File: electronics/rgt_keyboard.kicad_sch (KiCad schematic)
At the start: 61 parts, among them J5 Conn_01x05_Female, J6 Conn_01x05_Male, SW30 SW_SPST, SW31 SW_SPST, SW32 SW_SPST, SW33 SW_SPST, SW34 SW_SPST, SW35 SW_SPST, SW36 SW_SPST, SW37 SW_SPST, SW38 SW_SPST, SW39 SW_SPST, SW40 SW_SPST, SW41 SW_SPST, SW42 SW_SPST, SW43 SW_SPST, SW44 SW_SPST, SW45 SW_SPST, SW46 SW_SPST, SW47 SW_SPST, SW48 SW_SPST, SW49 SW_SPST, SW50 SW_SPST, SW51 SW_SPST, SW52 SW_SPST, SW53 SW_SPST, SW54 SW_SPST, SW55 SW_SPST, SW56 SW_SPST, SW57 SW_SPST, SW58 SW_SPST, U3 PCA9675PW

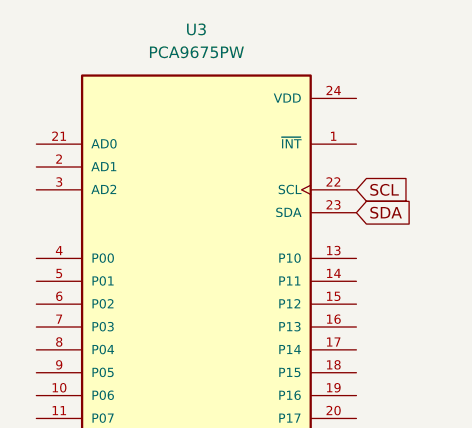
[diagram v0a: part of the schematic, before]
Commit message: fix right keyboard matrix
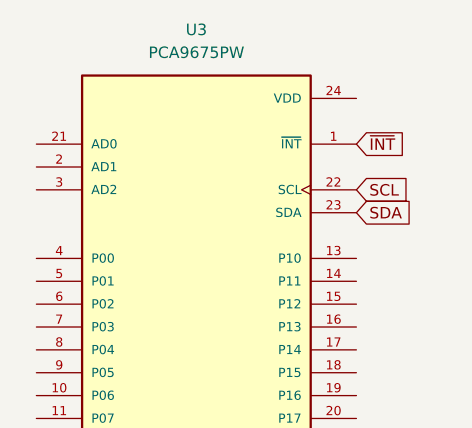
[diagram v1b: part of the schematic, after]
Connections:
- net ~{INT}: now also U3.1 (~{INT})
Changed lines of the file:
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@@
+    )
+  )
+  (global_label "~{INT}" (shape input) (at 246.38 34.29 0) (fields_autoplaced)
+    (effects (font (size 1.27 1.27)) (justify left))
+    (property "Intersheet References" "${INTERSHEET_REFS}" (id 0) (at 251.696 34.3694 0)
+      (effects (font (size 1.27 1.27)) (justify left) hide)
     )
   )

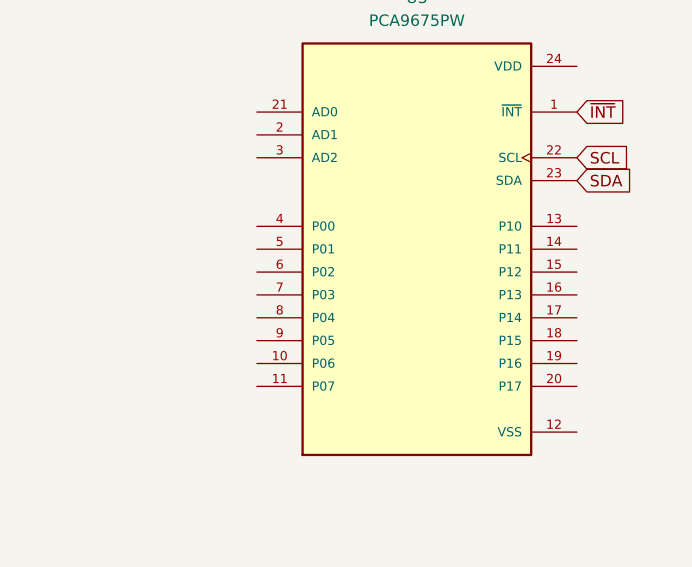
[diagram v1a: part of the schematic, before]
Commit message: connect matrix to io expander
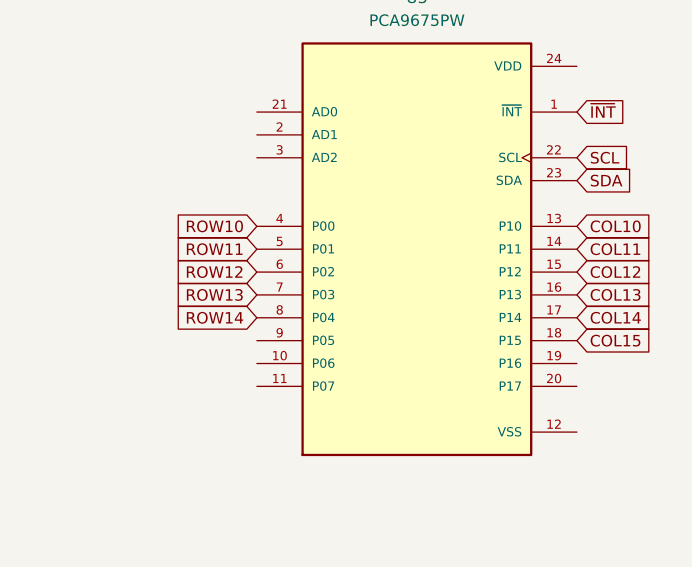
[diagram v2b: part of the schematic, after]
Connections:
- net COL10: now also U3.13 (P10)
- net COL11: now also U3.14 (P11)
- net COL12: now also U3.15 (P12)
- net COL13: now also U3.16 (P13)
- net COL14: now also U3.17 (P14)
- net COL15: now also U3.18 (P15)
- net ROW10: now also U3.4 (P00)
- net ROW11: now also U3.5 (P01)
- net ROW12: now also U3.6 (P02)
- net ROW13: now also U3.7 (P03)
- net ROW14: now also U3.8 (P04)
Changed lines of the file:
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@@
+    )
+  )
+  (global_label "COL10" (shape input) (at 246.38 46.99 0) (fields_autoplaced)
+    (effects (font (size 1.27 1.27)) (justify left))
+    (property "Intersheet References" "${INTERSHEET_REFS}" (id 0) (at 254.8407 47.0694 0)
+      (effects (font (size 1.27 1.27)) (justify left) hide)
     )
   )
@@
     )
   )
+  (global_label "COL14" (shape input) (at 246.38 57.15 0) (fields_autoplaced)
+    (effects (font (size 1.27 1.27)) (justify left))
+    (property "Intersheet References" "${INTERSHEET_REFS}" (id 0) (at 254.8407 57.2294 0)
+      (effects (font (size 1.27 1.27)) (justify left) hide)
+    )
+  )
   (global_label "ROW10" (shape input) (at 139.7 92.71 180) (fields_autoplaced)
     (effects (font (size 1.27 1.27)) (justify right))
@@
     )
   )
+  (global_label "ROW13" (shape input) (at 210.82 54.61 180) (fields_autoplaced)
+    (effects (font (size 1.27 1.27)) (justify right))
+    (property "Intersheet References" "${INTERSHEET_REFS}" (id 0) (at 201.9359 54.5306 0)
+      (effects (font (size 1.27 1.27)) (justify right) hide)
+    )
+  )
   (global_label "ROW12" (shape input) (at 78.74 124.46 180) (fields_autoplaced)
     (effects (font (size 1.27 1.27)) (justify right))
@@
     )
   )
+  (global_label "ROW12" (shape input) (at 210.82 52.07 180) (fields_autoplaced)
+    (effects (font (size 1.27 1.27)) (justify right))
+    (property "Intersheet References" "${INTERSHEET_REFS}" (id 0) (at 201.9359 51.9906 0)
+      (effects (font (size 1.27 1.27)) (justify right) hide)
+    )
+  )
   (global_label "ROW12" (shape input) (at 119.38 124.46 180) (fields_autoplaced)
     (effects (font (size 1.27 1.27)) (justify right))
@@
     )
   )
+  (global_label "COL13" (shape input) (at 246.38 54.61 0) (fields_autoplaced)
+    (effects (font (size 1.27 1.27)) (justify left))
+    (property "Intersheet References" "${INTERSHEET_REFS}" (id 0) (at 254.8407 54.6894 0)
+      (effects (font (size 1.27 1.27)) (justify left) hide)
+    )
+  )
   (global_label "~{INT}" (shape input) (at 246.38 34.29 0) (fields_autoplaced)
     (effects (font (size 1.27 1.27)) (justify left))
@@
     )
   )
+  (global_label "ROW10" (shape input) (at 210.82 46.99 180) (fields_autoplaced)
+    (effects (font (size 1.27 1.27)) (justify right))
+    (property "Intersheet References" "${INTERSHEET_REFS}" (id 0) (at 201.9359 46.9106 0)
+      (effects (font (size 1.27 1.27)) (justify right) hide)
+    )
+  )
+  (global_label "ROW14" (shape input) (at 210.82 57.15 180) (fields_autoplaced)
+    (effects (font (size 1.27 1.27)) (justify right))
+    (property "Intersheet References" "${INTERSHEET_REFS}" (id 0) (at 201.9359 57.0706 0)
+      (effects (font (size 1.27 1.27)) (justify right) hide)
+    )
+  )
   (global_label "ROW11" (shape input) (at 58.42 107.95 180) (fields_autoplaced)
     (effects (font (size 1.27 1.27)) (justify right))
@@
     )
   )
+  (global_label "COL12" (shape input) (at 246.38 52.07 0) (fields_autoplaced)
+    (effects (font (size 1.27 1.27)) (justify left))
+    (property "Intersheet References" "${INTERSHEET_REFS}" (id 0) (at 254.8407 52.1494 0)
+      (effects (font (size 1.27 1.27)) (justify left) hide)
+    )
+  )
+  (global_label "ROW11" (shape input) (at 210.82 49.53 180) (fields_autoplaced)
+    (effects (font (size 1.27 1.27)) (justify right))
+    (property "Intersheet References" "${INTERSHEET_REFS}" (id 0) (at 201.9359 49.4506 0)
+      (effects (font (size 1.27 1.27)) (justify right) hide)
+    )
+  )
   (global_label "ROW13" (shape input) (at 119.38 140.97 180) (fields_autoplaced)
     (effects (font (size 1.27 1.27)) (justify right))
@@
     )
   )
+  (global_label "COL15" (shape input) (at 246.38 59.69 0) (fields_autoplaced)
+    (effects (font (size 1.27 1.27)) (justify left))
+    (property "Intersheet References" "${INTERSHEET_REFS}" (id 0) (at 254.8407 59.7694 0)
+      (effects (font (size 1.27 1.27)) (justify left) hide)
+    )
+  )
   (global_label "ROW10" (shape input) (at 38.1 92.71 180) (fields_autoplaced)
     (effects (font (size 1.27 1.27)) (justify right))
@@
     )
   )
+  (global_label "COL11" (shape input) (at 246.38 49.53 0) (fields_autoplaced)
+    (effects (font (size 1.27 1.27)) (justify left))
+    (property "Intersheet References" "${INTERSHEET_REFS}" (id 0) (at 254.8407 49.6094 0)
+      (effects (font (size 1.27 1.27)) (justify left) hide)
+    )
+  )

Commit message: finish matrix
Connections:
- net COL10: now also U3.18 (P15); no longer U3.13 (P10)
- net COL11: now also U3.17 (P14); no longer U3.14 (P11)
- net COL12: now also U3.16 (P13); no longer U3.15 (P12)
- net COL13: now also U3.15 (P12); no longer U3.16 (P13)
- net COL14: now also U3.14 (P11); no longer U3.17 (P14)
- net COL15: now also U3.13 (P10); no longer U3.18 (P15)
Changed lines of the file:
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@@
     (stroke (width 0) (type default) (color 0 0 0 0))
   )
+  (global_label "COL15" (shape input) (at 246.38 46.99 0) (fields_autoplaced)
+    (effects (font (size 1.27 1.27)) (justify left))
+    (property "Intersheet References" "${INTERSHEET_REFS}" (id 0) (at 254.8407 46.9106 0)
+      (effects (font (size 1.27 1.27)) (justify left) hide)
+    )
+  )
   (global_label "~{INT}" (shape input) (at 240.03 124.46 0) (fields_autoplaced)
     (effects (font (size 1.27 1.27)) (justify left))
@@
     )
   )
-  (global_label "COL10" (shape input) (at 246.38 46.99 0) (fields_autoplaced)
-    (effects (font (size 1.27 1.27)) (justify left))
-    (property "Intersheet References" "${INTERSHEET_REFS}" (id 0) (at 254.8407 47.0694 0)
-      (effects (font (size 1.27 1.27)) (justify left) hide)
-    )
-  )
   (global_label "ROW14" (shape input) (at 38.1 156.21 180) (fields_autoplaced)
     (effects (font (size 1.27 1.27)) (justify right))
@@
     )
   )
+  (global_label "COL12" (shape input) (at 246.38 54.61 0) (fields_autoplaced)
+    (effects (font (size 1.27 1.27)) (justify left))
+    (property "Intersheet References" "${INTERSHEET_REFS}" (id 0) (at 254.8407 54.5306 0)
+      (effects (font (size 1.27 1.27)) (justify left) hide)
+    )
+  )
   (global_label "COL15" (shape input) (at 149.86 83.82 180) (fields_autoplaced)
     (effects (font (size 1.27 1.27)) (justify right))
@@
     )
   )
-  (global_label "COL14" (shape input) (at 246.38 57.15 0) (fields_autoplaced)
-    (effects (font (size 1.27 1.27)) (justify left))
-    (property "Intersheet References" "${INTERSHEET_REFS}" (id 0) (at 254.8407 57.2294 0)
-      (effects (font (size 1.27 1.27)) (justify left) hide)
-    )
-  )
   (global_label "ROW10" (shape input) (at 139.7 92.71 180) (fields_autoplaced)
     (effects (font (size 1.27 1.27)) (justify right))
@@
     )
   )
+  (global_label "COL14" (shape input) (at 246.38 49.53 0) (fields_autoplaced)
+    (effects (font (size 1.27 1.27)) (justify left))
+    (property "Intersheet References" "${INTERSHEET_REFS}" (id 0) (at 254.8407 49.4506 0)
+      (effects (font (size 1.27 1.27)) (justify left) hide)
+    )
+  )
   (global_label "ROW12" (shape input) (at 78.74 124.46 180) (fields_autoplaced)
     (effects (font (size 1.27 1.27)) (justify right))
@@
     )
   )
-  (global_label "COL13" (shape input) (at 246.38 54.61 0) (fields_autoplaced)
-    (effects (font (size 1.27 1.27)) (justify left))
-    (property "Intersheet References" "${INTERSHEET_REFS}" (id 0) (at 254.8407 54.6894 0)
-      (effects (font (size 1.27 1.27)) (justify left) hide)
-    )
-  )
   (global_label "~{INT}" (shape input) (at 246.38 34.29 0) (fields_autoplaced)
     (effects (font (size 1.27 1.27)) (justify left))
@@
     )
   )
+  (global_label "COL11" (shape input) (at 246.38 57.15 0) (fields_autoplaced)
+    (effects (font (size 1.27 1.27)) (justify left))
+    (property "Intersheet References" "${INTERSHEET_REFS}" (id 0) (at 254.8407 57.0706 0)
+      (effects (font (size 1.27 1.27)) (justify left) hide)
+    )
+  )
   (global_label "ROW11" (shape input) (at 139.7 107.95 180) (fields_autoplaced)
     (effects (font (size 1.27 1.27)) (justify right))
@@
     )
   )
-  (global_label "COL12" (shape input) (at 246.38 52.07 0) (fields_autoplaced)
-    (effects (font (size 1.27 1.27)) (justify left))
-    (property "Intersheet References" "${INTERSHEET_REFS}" (id 0) (at 254.8407 52.1494 0)
-      (effects (font (size 1.27 1.27)) (justify left) hide)
-    )
-  )
   (global_label "ROW11" (shape input) (at 210.82 49.53 180) (fields_autoplaced)
     (effects (font (size 1.27 1.27)) (justify right))
@@
     )
   )
-  (global_label "COL15" (shape input) (at 246.38 59.69 0) (fields_autoplaced)
-    (effects (font (size 1.27 1.27)) (justify left))
-    (property "Intersheet References" "${INTERSHEET_REFS}" (id 0) (at 254.8407 59.7694 0)
-      (effects (font (size 1.27 1.27)) (justify left) hide)
-    )
-  )
   (global_label "ROW10" (shape input) (at 38.1 92.71 180) (fields_autoplaced)
     (effects (font (size 1.27 1.27)) (justify right))
@@
     )
   )
-  (global_label "COL11" (shape input) (at 246.38 49.53 0) (fields_autoplaced)
-    (effects (font (size 1.27 1.27)) (justify left))
-    (property "Intersheet References" "${INTERSHEET_REFS}" (id 0) (at 254.8407 49.6094 0)
-      (effects (font (size 1.27 1.27)) (justify left) hide)
-    )
-  )
   (global_label "ROW14" (shape input) (at 99.06 156.21 180) (fields_autoplaced)
     (effects (font (size 1.27 1.27)) (justify right))
@@
     )
   )
+  (global_label "COL10" (shape input) (at 246.38 59.69 0) (fields_autoplaced)
+    (effects (font (size 1.27 1.27)) (justify left))
+    (property "Intersheet References" "${INTERSHEET_REFS}" (id 0) (at 254.8407 59.6106 0)
+      (effects (font (size 1.27 1.27)) (justify left) hide)
+    )
+  )
   (global_label "ROW14" (shape input) (at 119.38 156.21 180) (fields_autoplaced)
     (effects (font (size 1.27 1.27)) (justify right))
@@
     )
   )
+  (global_label "COL13" (shape input) (at 246.38 52.07 0) (fields_autoplaced)
+    (effects (font (size 1.27 1.27)) (justify left))
+    (property "Intersheet References" "${INTERSHEET_REFS}" (id 0) (at 254.8407 51.9906 0)
+      (effects (font (size 1.27 1.27)) (justify left) hide)
+    )
+  )

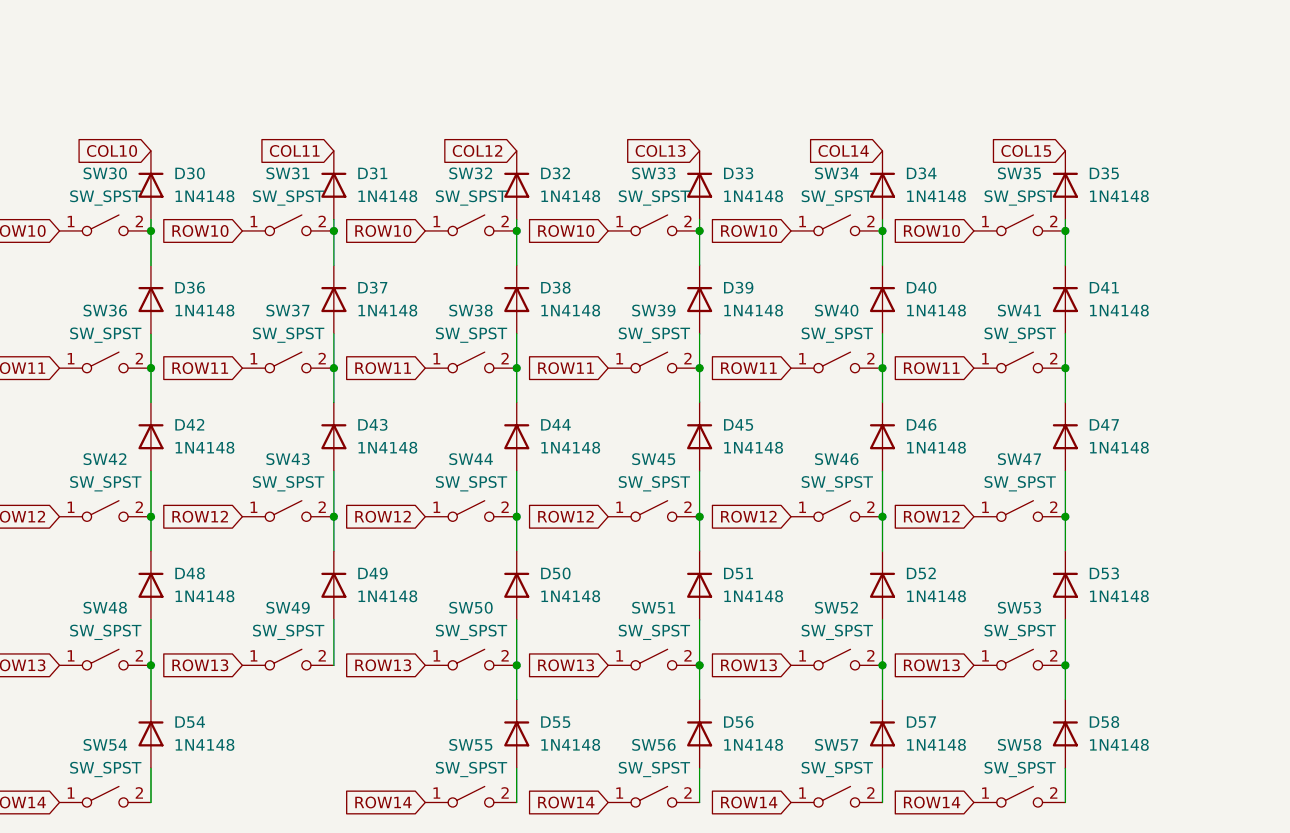
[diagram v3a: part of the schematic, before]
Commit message: update diode libraries
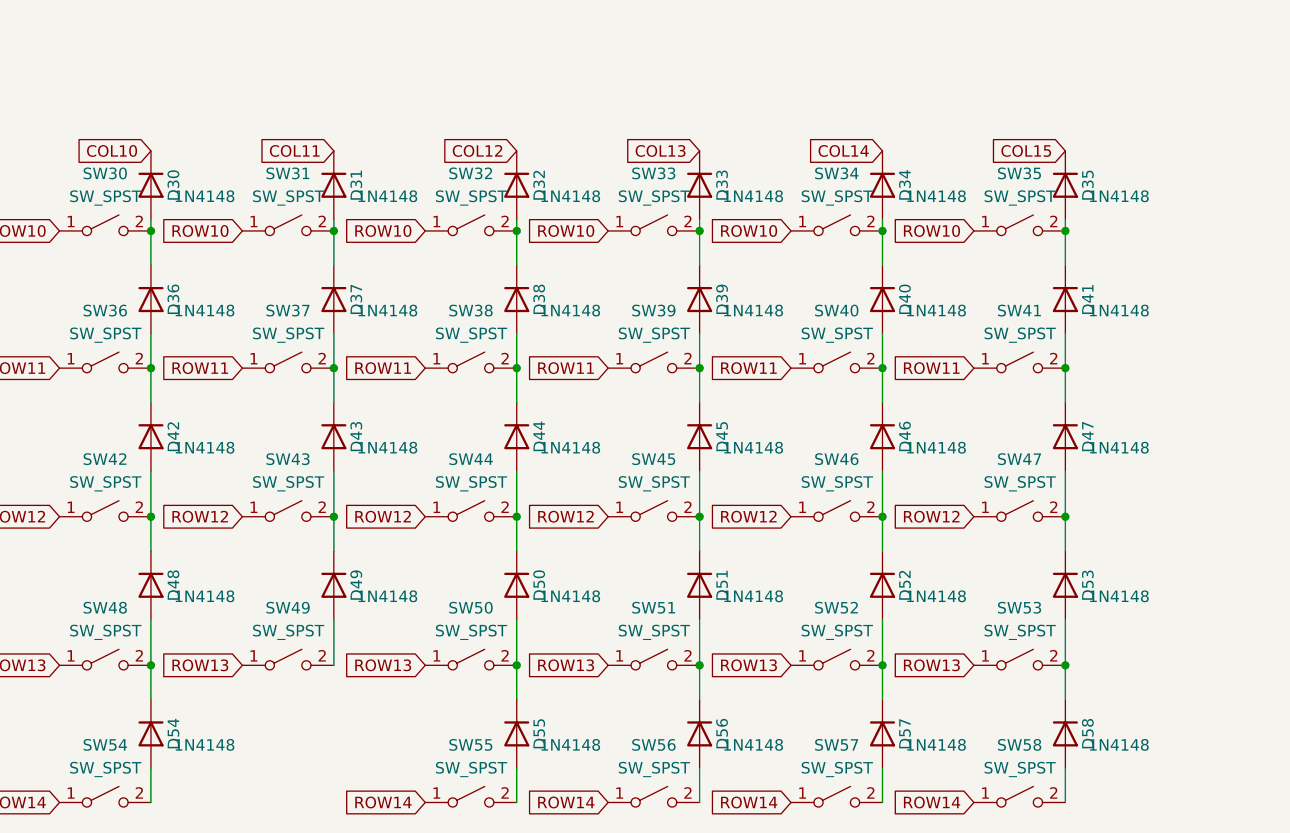
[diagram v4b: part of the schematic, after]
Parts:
- D30, D31, D32, D33, D34, D35, D36, D37, D38, D39, D40, D41, D42, D43, D44, D45, D46, D47, D48, D49, D50, D51, D52, D53, D54, D55, D56, D57, D58: footprint Diode_SMD:D_SOD-123 -> Diode_THT:D_DO-35_SOD27_P7.62mm_Horizontal; symbol Diode:1N4148W -> 1N4148:1N4148

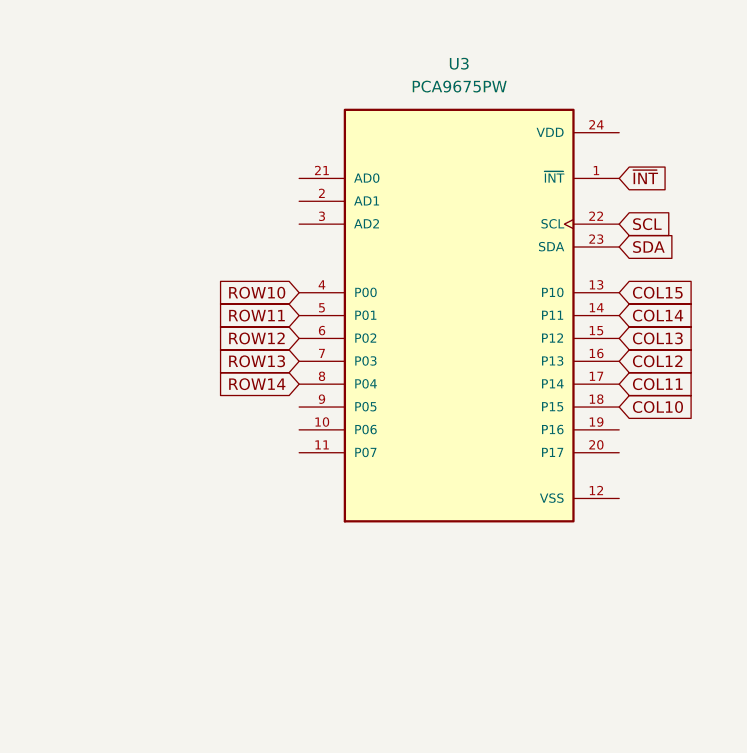
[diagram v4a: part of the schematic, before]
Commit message: add power and i2c addressing
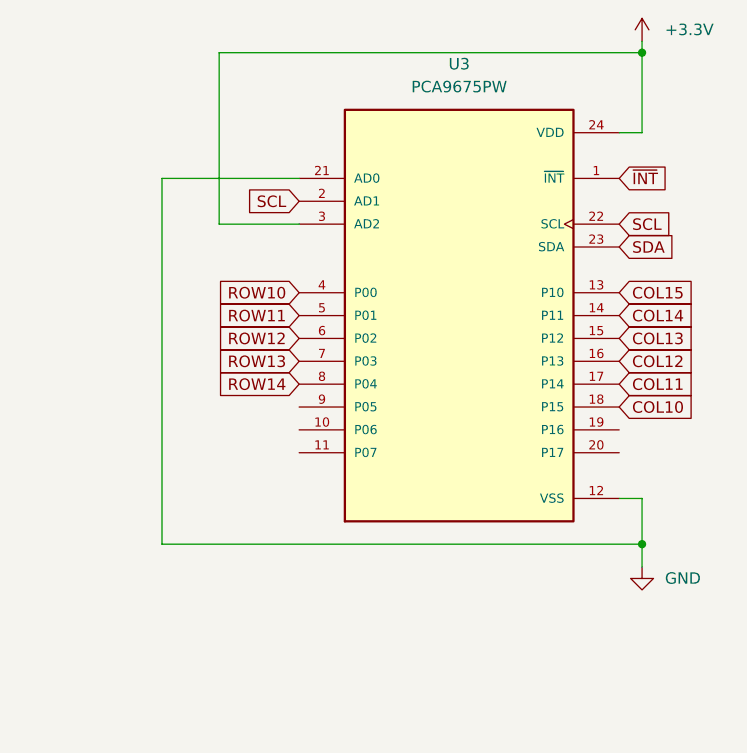
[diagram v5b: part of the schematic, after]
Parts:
- D30, D31, D32, D33, D34, D35, D36, D37, D38, D39, D40, D41, D42, D43, D44, D45, D46, D47, D48, D49, D50, D51, D52, D53, D54, D55, D56, D57, D58: footprint Diode_THT:D_DO-35_SOD27_P7.62mm_Horizontal -> 1N4148:1N4148
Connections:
- net +3V3: now also U3.24 (VDD), U3.3 (AD2)
- net GND: now also U3.12 (VSS), U3.21 (AD0)
- net SCL: now also U3.2 (AD1)
